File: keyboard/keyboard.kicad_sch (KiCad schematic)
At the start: 91 parts, among them IC1 NRF54L15-QFAA-R, IC2 NPM1300-QEAA-R7, J1 Conn_02x03_Counter_Clockwise

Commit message: ~finished schematic, started layout
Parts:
- removed IC1: NRF54L15-QFAA-R, QFN40P600X600X95-49N, symbol SamacSys_Parts:NRF54L15-QFAA-R
- added C1, C3, C4: 10uf, Capacitor_SMD:C_0805_2012Metric_Pad1.18x1.45mm_HandSolder, symbol Device:C
- added C2: 1uf, Capacitor_SMD:C_0805_2012Metric_Pad1.18x1.45mm_HandSolder, symbol Device:C
- added C5: 100nf, Capacitor_SMD:C_0805_2012Metric_Pad1.18x1.45mm_HandSolder, symbol Device:C
- added D1: CHRG_LED, LED_SMD:LED_0805_2012Metric_Pad1.15x1.40mm_HandSolder, symbol Device:LED
- added D2, D3, D4, D5: LED, LED_SMD:LED_0805_2012Metric_Pad1.15x1.40mm_HandSolder, symbol Device:LED
- added J10, J11, J12, J13, J14, J15, J16, J17, J18, J19, J20, J21, J22, J4, J5, J6, J7, J8, J9: Conn_01x01, Connector_Wire:SolderWirePad_1x01_SMD_1x2mm, symbol Connector_Generic:Conn_01x01
- added J2: disp, Connector_PinHeader_2.54mm:PinHeader_1x04_P2.54mm_Vertical, symbol Connector_Generic:Conn_01x04
- added J3: BAT, Connector_PinHeader_2.54mm:PinHeader_1x02_P2.54mm_Vertical, symbol Connector_Generic:Conn_01x02
- added L1: L, Inductor_SMD:L_1008_2520Metric_Pad1.43x2.20mm_HandSolder, symbol Device:L
- added Q1: FS8205A, FS8205A:SOP65P640X120-8N, symbol FS8205A:FS8205A
- added R1: 300k, Resistor_SMD:R_0805_2012Metric_Pad1.20x1.40mm_HandSolder, symbol Device:R
- added R2: 1K, Resistor_SMD:R_0805_2012Metric_Pad1.20x1.40mm_HandSolder, symbol Device:R
- added R3: 100R, Resistor_SMD:R_0805_2012Metric_Pad1.20x1.40mm_HandSolder, symbol Device:R
- added R4, R5, R6, R7: 1k, Resistor_SMD:R_0805_2012Metric_Pad1.20x1.40mm_HandSolder, symbol Device:R
- added U1: ~, mylib:nrf54l15_holyiot, symbol mylib:nrf54l15_holyiot
- added U2: DW01A, Package_TO_SOT_SMD:SOT-23-6, symbol Battery_Management:DW01A
- added U3: USBC20, my_usbc:USBC_6PIN, symbol USBC20:USBC20
- IC2: footprint QFN50P500X500X90-33N -> mylib:QFN50P500X500X90-33N
- J1: value Conn_02x03_Counter_Clockwise -> PROG; footprint (none) -> mylib:SWD_PROG_5pin
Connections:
- net 3V3: now also IC2.12 (VDDIO), IC2.32 (VOUT2), C3.1, C3.2, C4.1, C5.1, J2.3 (Pin_3), L1.2, R4.1, R5.1, R6.1, R7.1, U1.4 (VDD), U1.9 (VDDM)
- net GND: now also IC2.17 (VSET1), IC2.18 (NTC), IC2.2 (PVSS1), IC2.29 (LSOUT1/VOUTLDO1), IC2.33 (AVSS), IC2.6 (PVSS2), C1.1, C2.2, C4.2, C5.2, Q1.6, Q1.7, R1.2, R2.1, U1.1 (GND), U1.36 (GND), U3.A12 (GND), U3.B12 (GND)
- net at SW1:0.1 (a), SW1:1.1 (a), SW1:2.1 (a)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: now also U1.18 (P2.01)
- net at SW0:0.1 (a), SW0:1.1 (a), SW0:2.1 (a)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: now also U1.17 (P2.00)
- net at SW4:0.1 (a), SW4:1.1 (a), SW4:2.1 (a)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: now also U1.21 (P2.04)
- net at SW10:0.2 (b), SW10:1.2 (b), SW10:2.2 (b)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: now also U1.26 (P2.09)
- net at SW8:0.2 (b), SW8:1.2 (b), SW8:2.2 (b)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: now also U1.24 (P2.07)
- net at SW2:0.1 (a), SW2:1.1 (a), SW2:2.1 (a)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: now also U1.19 (P2.02)
- net at SW9:0.2 (b), SW9:1.2 (b), SW9:2.2 (b)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: now also U1.25 (P2.08)
- net at D5:0.2 (A), SW5:1.1 (a), SW6:0.2 (b)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: now also U1.22 (P2.05)
- net at SW7:0.2 (b), SW7:1.2 (b), SW7:2.2 (b)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: now also U1.23 (P2.06)
- net at SW11:0.2 (b), SW11:1.2 (b), SW11:2.2 (b)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: now also U1.27 (P2.10)
- net VSYS: now reaches IC2.1 (VOUT1)
- net VSYS: now also IC2.20 (VSYS), IC2.4 (PVDD), C1.2, D1.2 (A)
- net at IC2.10 (GPIO3): now also J15.1 (Pin_1)
- net at IC2.11 (GPIO4): now also J16.1 (Pin_1)
- net at IC2.13 (SDA): now also U1.6 (P1.12)
- net at IC2.14 (SCL): now also U1.5 (P1.11)
- net at IC2.16 (VSET2): now also R1.1
- net at IC2.19 (VBAT): now also J3.2 (Pin_2), R3.1
- net at IC2.21 (VBUS): now also U3.A9 (VBUS), U3.B9 (VBUS)
- net at IC2.22 (VBUSOUT): now also C2.1
- net at IC2.23 (CC1): now also U3.A5 (CC1)
- net at IC2.24 (CC2): now also U3.B5 (CC2)
- net at IC2.25 (LED0): now also D1.1 (K)
- net at IC2.26 (LED1): now also J22.1 (Pin_1)
- net at IC2.27 (LED2): now also J21.1 (Pin_1)
- net at IC2.28 (LSIN1/VINLDO1): now also J2.4 (Pin_4)
- net at IC2.30 (LSIN2/VINLDO2): now also J20.1 (Pin_1)
- net at IC2.31 (LSOUT2/VOUTLDO2): now also J19.1 (Pin_1)
- net at IC2.5 (SW2): now also L1.1
- net at IC2.7 (GPIO0): now also J18.1 (Pin_1)
- net at IC2.8 (GPIO1): now also J17.1 (Pin_1)
- net at IC2.9 (GPIO2): now also J14.1 (Pin_1)
- net at SW3:0.1 (a), SW3:1.1 (a), SW3:2.1 (a)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: now also U1.20 (P2.03)
- net at J1.2 (Pin_2): now also U1.31 (SWDIO)
- net at J1.3 (Pin_3): now also U1.30 (SWDCLK)
- net at J1.5 (Pin_5): now also U1.35 (NRESET)
- new net: D3.1 (K), U1.15 (P1.07)
- new net: D3.2 (A), R5.2
- new net: J3.1 (Pin_1), Q1.2, Q1.3, U2.6 (GND)
- new net: J8.1 (Pin_1), U1.28 (P0.00)
- new net: D2.2 (A), R4.2
- new net: D2.1 (K), U1.16 (P1.08)
- new net: J13.1 (Pin_1), U1.7 (P1.13)
- new net: J6.1 (Pin_1), U1.32 (P0.02)
- new net: J11.1 (Pin_1), U1.10 (P1.02)
- new net: J10.1 (Pin_1), U1.11 (P1.03)
- new net: J9.1 (Pin_1), U1.12 (P1.04)
- new net: D5.1 (K), U1.13 (P1.05)
- new net: D4.1 (K), U1.14 (P1.06)
- new net: J7.1 (Pin_1), U1.29 (P0.01)
- new net: J5.1 (Pin_1), U1.33 (P0.03)
- new net: J4.1 (Pin_1), U1.34 (P0.04)
- new net: J12.1 (Pin_1), U1.8 (P1.14)
- new net: R3.2, U2.5 (VCC)
- new net: D4.2 (A), R6.2
- new net: D5.2 (A), R7.2
- new net: R2.2, U2.2 (CS)
- new net: Q1.1, Q1.8
- new net: Q1.4, U2.1 (OD)
- new net: Q1.5, U2.3 (OC)
- new net disp_sck: J2.2 (Pin_2), U1.2 (P1.09)
- new net disp_sda: J2.1 (Pin_1), U1.3 (P1.10)
- no-connect marks 0 -> 3

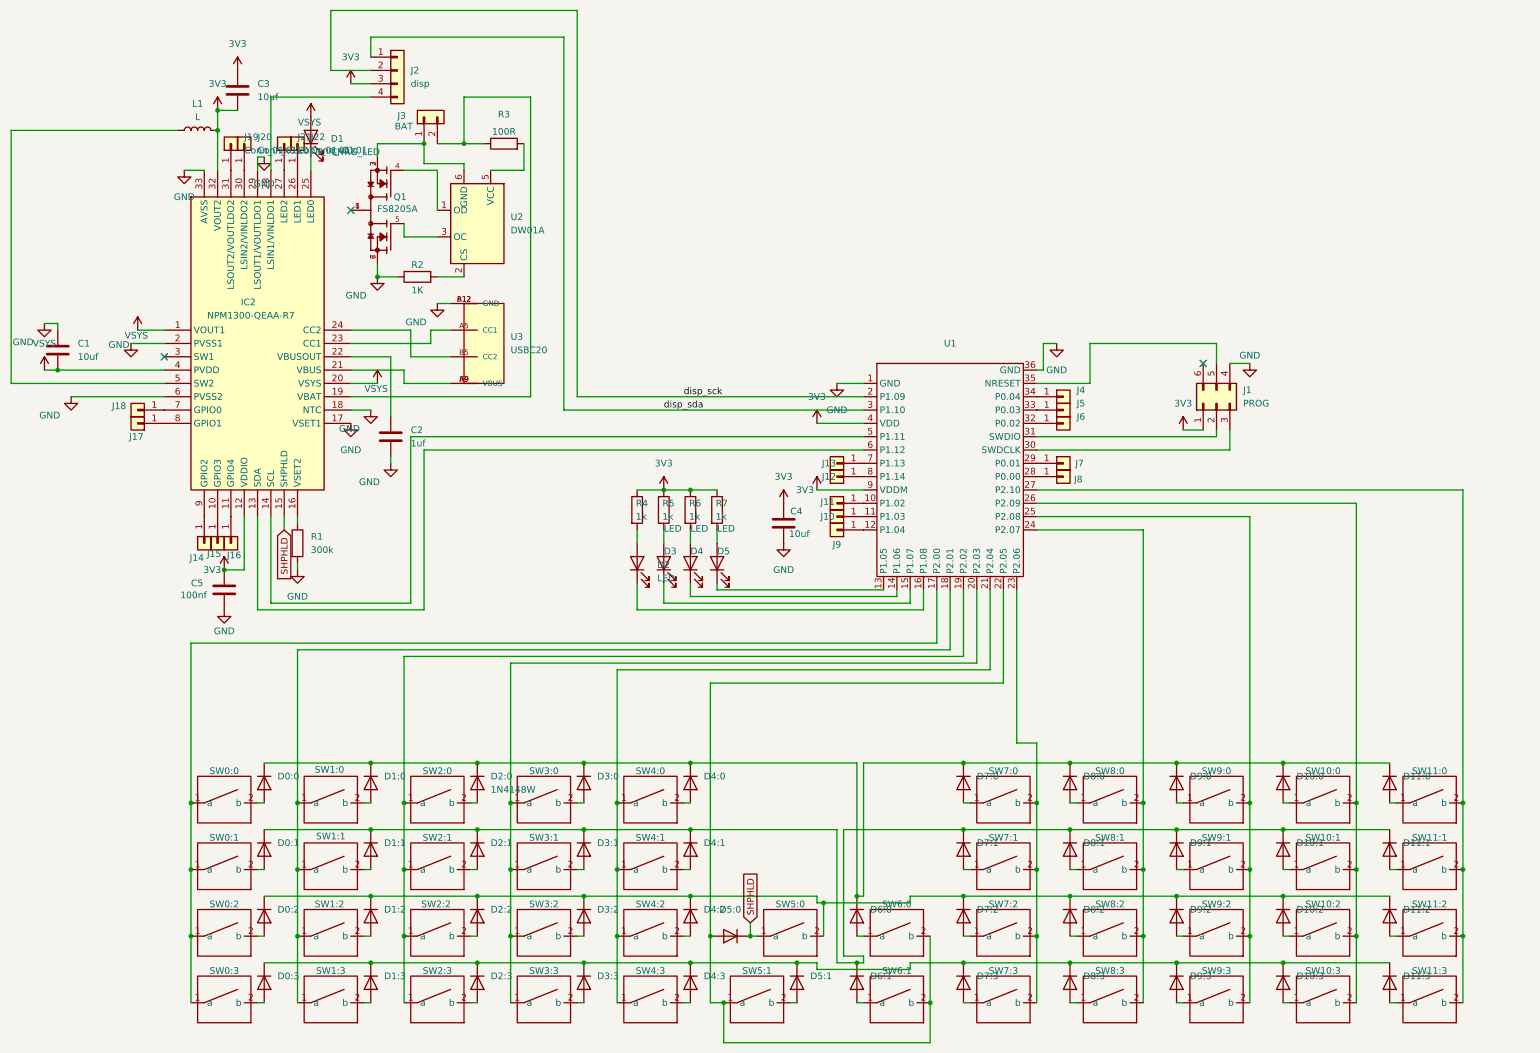
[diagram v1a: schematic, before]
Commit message: v1.0 PCB (jlcpcb order)
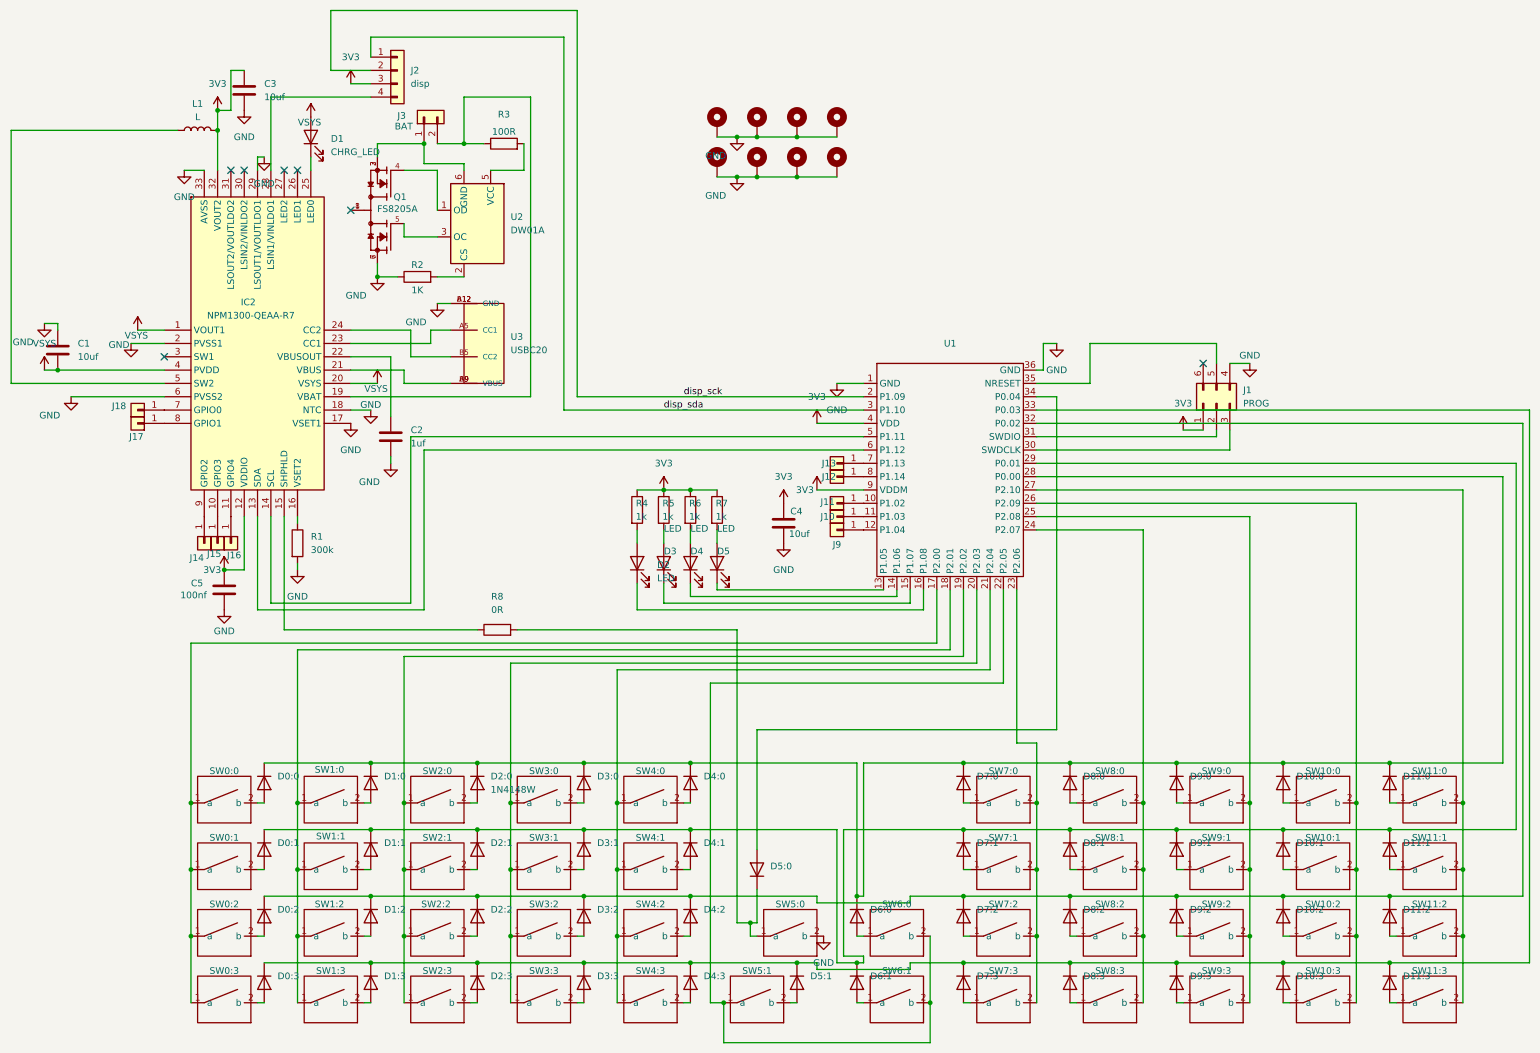
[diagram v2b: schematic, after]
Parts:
- removed J19, J20, J21, J22, J4, J5, J6, J7, J8: Conn_01x01, Connector_Wire:SolderWirePad_1x01_SMD_1x2mm, symbol Connector_Generic:Conn_01x01
- added H1, H2, H3, H4, H5, H6, H7, H8: MountingHole_Pad, MountingHole:MountingHole_2.2mm_M2_DIN965_Pad, symbol Mechanical:MountingHole_Pad
- added R8: 0R, Resistor_SMD:R_0805_2012Metric_Pad1.20x1.40mm_HandSolder, symbol Device:R
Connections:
- net 3V3: no longer C3.2
- net GND: now also C3.2, SW5:0.2 (b), H1.1, H2.1, H3.1, H4.1, H5.1, H6.1, H7.1, H8.1
- net at D0:1.1 (K), D10:1.1 (K), D11:1.1 (K)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: now also U1.29 (P0.01)
- net at D0:2.1 (K), D10:2.1 (K), D11:2.1 (K)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: now also U1.32 (P0.02); no longer SW5:0.2 (b)
- net at U1.28 (P0.00): now also D0:0.1 (K), D10:0.1 (K), D11:0.1 (K), D1:0.1 (K), D2:0.1 (K), D3:0.1 (K), D4:0.1 (K), D6:0.1 (K), D7:0.1 (K), D8:0.1 (K), D9:0.1 (K)
- net at D0:3.1 (K), D10:3.1 (K), D11:3.1 (K)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: now also U1.33 (P0.03)
- net at SW5:1.1 (a), SW6:0.2 (b), SW6:1.2 (b)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: no longer D5:0.2 (A)
- net at U1.34 (P0.04): now also D5:0.2 (A)
- net SHPHLD: no longer names the net of D5:0.1 (K), SW5:0.1 (a)
- net SHPHLD: now also R8.2; no longer IC2.15 (SHPHLD)
- new net: IC2.15 (SHPHLD), R8.1
- no-connect marks 3 -> 7
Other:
- moved on the sheet: C3, D5:0
